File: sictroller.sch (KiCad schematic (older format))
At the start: 12 parts

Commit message: Placement almost complete
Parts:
- removed W2, W3, W4: TEST_1P, Measurement_Points:Measurement_Point_Round-SMD-Pad_Small, symbol TEST_1P
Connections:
- no-connect marks 0 -> 1
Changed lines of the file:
@@
-$EndComp
-$Comp
-L TEST_1P W2
-U 1 1 57A8E4FF
-P 4250 2000
-F 0 "W2" H 4300 2150 50  0000 L CNN
-F 1 "TEST_1P" H 4308 2029 50  0001 L CNN
-F 2 "Measurement_Points:Measurement_Point_Round-SMD-Pad_Small" H 4450 2000 50  0001 C CNN
-F 3 "" H 4450 2000 50  0000 C CNN
-	1    4250 2000
-	1    0    0    -1
-$EndComp
-$Comp
-L TEST_1P W3
-U 1 1 57A8E7A8
-P 4400 2100
-F 0 "W3" H 4450 2250 50  0000 L CNN
-F 1 "TEST_1P" H 4458 2129 50  0001 L CNN
-F 2 "Measurement_Points:Measurement_Point_Round-SMD-Pad_Small" H 4600 2100 50  0001 C CNN
-F 3 "" H 4600 2100 50  0000 C CNN
-	1    4400 2100
-	1    0    0    -1
-$EndComp
-$Comp
-L TEST_1P W4
-U 1 1 57A8EA5A
-P 4550 2200
-F 0 "W4" H 4600 2350 50  0000 L CNN
-F 1 "TEST_1P" H 4608 2229 50  0001 L CNN
-F 2 "Measurement_Points:Measurement_Point_Round-SMD-Pad_Small" H 4750 2200 50  0001 C CNN
-F 3 "" H 4750 2200 50  0000 C CNN
-	1    4550 2200
-	1    0    0    -1
 $EndComp
 $Comp
@@
 	1    0    0    -1
 $EndComp
+NoConn ~ 2800 1200
 $EndSCHEMATC

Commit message: Initial placement ~complete
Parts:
- removed W6, W7: TEST_1P, Measurement_Points:Measurement_Point_Round-TH_Small, symbol TEST_1P
- removed W8: TEST_1P, Measurement_Points:Measurement_Point_Round-SMD-Pad_Small, symbol TEST_1P
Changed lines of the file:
@@
 $EndComp
-$Comp
-L TEST_1P W6
-U 1 1 57A85972
-P 7300 2350
-F 0 "W6" H 7350 2450 50  0000 L CNN
-F 1 "TEST_1P" H 7358 2379 50  0001 L CNN
-F 2 "Measurement_Points:Measurement_Point_Round-TH_Small" H 7500 2350 50  0001 C CNN
-F 3 "" H 7500 2350 50  0000 C CNN
-	1    7300 2350
-	1    0    0    -1
-$EndComp
-$Comp
-L TEST_1P W7
-U 1 1 57A89327
-P 7500 2450
-F 0 "W7" H 7550 2600 50  0000 L CNN
-F 1 "TEST_1P" H 7558 2479 50  0001 L CNN
-F 2 "Measurement_Points:Measurement_Point_Round-TH_Small" H 7700 2450 50  0001 C CNN
-F 3 "" H 7700 2450 50  0000 C CNN
-	1    7500 2450
-	1    0    0    -1
-$EndComp
-$Comp
-L TEST_1P W8
-U 1 1 57A89F70
-P 7300 2650
-F 0 "W8" H 7350 2800 50  0000 L CNN
-F 1 "TEST_1P" H 7358 2679 50  0001 L CNN
-F 2 "Measurement_Points:Measurement_Point_Round-SMD-Pad_Small" H 7500 2650 50  0001 C CNN
-F 3 "" H 7500 2650 50  0000 C CNN
-	1    7300 2650
-	-1   0    0    1
-$EndComp
-Connection ~ 7300 2650
-Connection ~ 7500 2450
-Connection ~ 7300 2350
 $Comp
 L TEST_1P W1

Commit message: Add fiducials
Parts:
- added FID1, FID10, FID11, FID12, FID13, FID14, FID15, FID16, FID2, FID3, FID4, FID5, FID6, FID7, FID8, FID9, FID? (x4): Fiducial, sictroller:Fiducial_1mm_CopperTop, symbol Fiducial
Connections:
- no-connect marks 1 -> 0
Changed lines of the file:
@@
 $EndComp
 $Comp
-L GNDD #PWR1
+L GNDD #PWR01
 U 1 1 57A83FCA
 P 800 7550
-F 0 "#PWR1" H 800 7300 50  0001 C CNN
+F 0 "#PWR01" H 800 7300 50  0001 C CNN
 F 1 "GNDD" H 805 7377 50  0000 C CNN
 F 2 "" H 800 7550 50  0000 C CNN
@@
 $EndComp
 $Comp
-L GNDD #PWR2
+L GNDD #PWR02
 U 1 1 57A844D3
 P 1200 7550
-F 0 "#PWR2" H 1200 7300 50  0001 C CNN
+F 0 "#PWR02" H 1200 7300 50  0001 C CNN
 F 1 "GNDD" H 1205 7377 50  0000 C CNN
 F 2 "" H 1200 7550 50  0000 C CNN
@@
 Connection ~ 4100 2350
 $Comp
-L GNDA #PWR4
+L GNDA #PWR03
 U 1 1 5806E9BD
 P 2000 7550
-F 0 "#PWR4" H 2000 7300 50  0001 C CNN
+F 0 "#PWR03" H 2000 7300 50  0001 C CNN
 F 1 "GNDA" H 2000 7400 50  0000 C CNN
 F 2 "" H 2000 7550 50  0000 C CNN
@@
 $EndComp
 $Comp
-L GNDA #PWR3
+L GNDA #PWR04
 U 1 1 5806ED9E
 P 1600 7550
-F 0 "#PWR3" H 1600 7300 50  0001 C CNN
+F 0 "#PWR04" H 1600 7300 50  0001 C CNN
 F 1 "GNDA" H 1600 7400 50  0000 C CNN
 F 2 "" H 1600 7550 50  0000 C CNN
@@
 	1    0    0    -1
 $EndComp
-NoConn ~ 2800 1200
+$Comp
+L Fiducial FID1
+U 1 1 580C9076
+P 1950 4550
+F 0 "FID1" H 1960 4580 60  0000 C CNN
+F 1 "Fiducial" H 1940 4480 60  0000 C CNN
+F 2 "sictroller:Fiducial_1mm_CopperTop" H 1950 4550 60  0001 C CNN
+F 3 "" H 1950 4550 60  0001 C CNN
+	1    1950 4550
+	1    0    0    -1
+$EndComp
+$Comp
+L Fiducial FID2
+U 1 1 580C9CFA
+P 2550 4550
+F 0 "FID2" H 2560 4580 60  0000 C CNN
+F 1 "Fiducial" H 2540 4480 60  0000 C CNN
+F 2 "sictroller:Fiducial_1mm_CopperTop" H 2550 4550 60  0001 C CNN
+F 3 "" H 2550 4550 60  0001 C CNN
+	1    2550 4550
+	1    0    0    -1
+$EndComp
+$Comp
+L Fiducial FID3
+U 1 1 580CA196
+P 3150 4550
+F 0 "FID3" H 3160 4580 60  0000 C CNN
+F 1 "Fiducial" H 3140 4480 60  0000 C CNN
+F 2 "sictroller:Fiducial_1mm_CopperTop" H 3150 4550 60  0001 C CNN
+F 3 "" H 3150 4550 60  0001 C CNN
+	1    3150 4550
+	1    0    0    -1
+$EndComp
+$Comp
+L Fiducial FID4
+U 1 1 580CA19C
+P 3750 4550
+F 0 "FID4" H 3760 4580 60  0000 C CNN
+F 1 "Fiducial" H 3740 4480 60  0000 C CNN
+F 2 "sictroller:Fiducial_1mm_CopperTop" H 3750 4550 60  0001 C CNN
+F 3 "" H 3750 4550 60  0001 C CNN
+	1    3750 4550
+	1    0    0    -1
+$EndComp
+$Comp
+L Fiducial FID7
+U 1 1 580CA452
+P 3150 4950
+F 0 "FID7" H 3160 4980 60  0000 C CNN
+F 1 "Fiducial" H 3140 4880 60  0000 C CNN
+F 2 "sictroller:Fiducial_1mm_CopperTop" H 3150 4950 60  0001 C CNN
+F 3 "" H 3150 4950 60  0001 C CNN
+	1    3150 4950
+	1    0    0    -1
+$EndComp
+$Comp
+L Fiducial FID8
+U 1 1 580CA458
+P 3750 4950
+F 0 "FID8" H 3760 4980 60  0000 C CNN
+F 1 "Fiducial" H 3740 4880 60  0000 C CNN
+F 2 "sictroller:Fiducial_1mm_CopperTop" H 3750 4950 60  0001 C CNN
+F 3 "" H 3750 4950 60  0001 C CNN
+	1    3750 4950
+	1    0    0    -1
+$EndComp
+$Comp
+L Fiducial FID5
+U 1 1 580CA6D6
+P 1950 4950
+F 0 "FID5" H 1960 4980 60  0000 C CNN
+F 1 "Fiducial" H 1940 4880 60  0000 C CNN
+F 2 "sictroller:Fiducial_1mm_CopperTop" H 1950 4950 60  0001 C CNN
+F 3 "" H 1950 4950 60  0001 C CNN
+	1    1950 4950
+	1    0    0    -1
+$EndComp
+$Comp
+L Fiducial FID6
+U 1 1 580CA6DC
+P 2550 4950
+F 0 "FID6" H 2560 4980 60  0000 C CNN
+F 1 "Fiducial" H 2540 4880 60  0000 C CNN
+F 2 "sictroller:Fiducial_1mm_CopperTop" H 2550 4950 60  0001 C CNN
+F 3 "" H 2550 4950 60  0001 C CNN
+	1    2550 4950
+	1    0    0    -1
+$EndComp
+$Comp
+L Fiducial FID11
+U 1 1 580CC37C
+P 3150 5350
+F 0 "FID11" H 3160 5380 60  0000 C CNN
+F 1 "Fiducial" H 3140 5280 60  0000 C CNN
+F 2 "sictroller:Fiducial_1mm_CopperTop" H 3150 5350 60  0001 C CNN
+F 3 "" H 3150 5350 60  0001 C CNN
+	1    3150 5350
+	1    0    0    -1
+$EndComp
+$Comp
+L Fiducial FID12
+U 1 1 580CC382
+P 3750 5350
+F 0 "FID12" H 3760 5380 60  0000 C CNN
+F 1 "Fiducial" H 3740 5280 60  0000 C CNN
+F 2 "sictroller:Fiducial_1mm_CopperTop" H 3750 5350 60  0001 C CNN
+F 3 "" H 3750 5350 60  0001 C CNN
+	1    3750 5350
+	1    0    0    -1
+$EndComp
+$Comp
+L Fiducial FID9
+U 1 1 580CC388
+P 1950 5350
+F 0 "FID9" H 1960 5380 60  0000 C CNN
+F 1 "Fiducial" H 1940 5280 60  0000 C CNN
+F 2 "sictroller:Fiducial_1mm_CopperTop" H 1950 5350 60  0001 C CNN
+F 3 "" H 1950 5350 60  0001 C CNN
+	1    1950 5350
+	1    0    0    -1
+$EndComp
+$Comp
+L Fiducial FID10
+U 1 1 580CC38E
+P 2550 5350
+F 0 "FID10" H 2560 5380 60  0000 C CNN
+F 1 "Fiducial" H 2540 5280 60  0000 C CNN
+F 2 "sictroller:Fiducial_1mm_CopperTop" H 2550 5350 60  0001 C CNN
+F 3 "" H 2550 5350 60  0001 C CNN
+	1    2550 5350
+	1    0    0    -1
+$EndComp
+$Comp
+L Fiducial FID15
+U 1 1 580CCCE0
+P 3150 5750
+F 0 "FID15" H 3160 5780 60  0000 C CNN
+F 1 "Fiducial" H 3140 5680 60  0000 C CNN
+F 2 "sictroller:Fiducial_1mm_CopperTop" H 3150 5750 60  0001 C CNN
+F 3 "" H 3150 5750 60  0001 C CNN
+	1    3150 5750
+	1    0    0    -1
+$EndComp
+$Comp
+L Fiducial FID16
+U 1 1 580CCCE6
+P 3750 5750
+F 0 "FID16" H 3760 5780 60  0000 C CNN
+F 1 "Fiducial" H 3740 5680 60  0000 C CNN
+F 2 "sictroller:Fiducial_1mm_CopperTop" H 3750 5750 60  0001 C CNN
+F 3 "" H 3750 5750 60  0001 C CNN
+	1    3750 5750
+	1    0    0    -1
+$EndComp
+$Comp
+L Fiducial FID13
+U 1 1 580CCCEC
+P 1950 5750
+F 0 "FID13" H 1960 5780 60  0000 C CNN
+F 1 "Fiducial" H 1940 5680 60  0000 C CNN
+F 2 "sictroller:Fiducial_1mm_CopperTop" H 1950 5750 60  0001 C CNN
+F 3 "" H 1950 5750 60  0001 C CNN
+	1    1950 5750
+	1    0    0    -1
+$EndComp
+$Comp
+L Fiducial FID14
+U 1 1 580CCCF2
+P 2550 5750
+F 0 "FID14" H 2560 5780 60  0000 C CNN
+F 1 "Fiducial" H 2540 5680 60  0000 C CNN
+F 2 "sictroller:Fiducial_1mm_CopperTop" H 2550 5750 60  0001 C CNN
+F 3 "" H 2550 5750 60  0001 C CNN
+	1    2550 5750
+	1    0    0    -1
+$EndComp
+$Comp
+L Fiducial FID?
+U 1 1 580CDCBE
+P 3150 6150
+F 0 "FID?" H 3160 6180 60  0000 C CNN
+F 1 "Fiducial" H 3140 6080 60  0000 C CNN
+F 2 "sictroller:Fiducial_1mm_CopperTop" H 3150 6150 60  0001 C CNN
+F 3 "" H 3150 6150 60  0001 C CNN
+	1    3150 6150
+	1    0    0    -1
+$EndComp
+$Comp
+L Fiducial FID?
+U 1 1 580CDCC4
+P 3750 6150
+F 0 "FID?" H 3760 6180 60  0000 C CNN
+F 1 "Fiducial" H 3740 6080 60  0000 C CNN
+F 2 "sictroller:Fiducial_1mm_CopperTop" H 3750 6150 60  0001 C CNN
+F 3 "" H 3750 6150 60  0001 C CNN
+	1    3750 6150
+	1    0    0    -1
+$EndComp
+$Comp
+L Fiducial FID?
+U 1 1 580CDCCA
+P 1950 6150
+F 0 "FID?" H 1960 6180 60  0000 C CNN
+F 1 "Fiducial" H 1940 6080 60  0000 C CNN
+F 2 "sictroller:Fiducial_1mm_CopperTop" H 1950 6150 60  0001 C CNN
+F 3 "" H 1950 6150 60  0001 C CNN
+	1    1950 6150
+	1    0    0    -1
+$EndComp
+$Comp
+L Fiducial FID?
+U 1 1 580CDCD0
+P 2550 6150
+F 0 "FID?" H 2560 6180 60  0000 C CNN
+F 1 "Fiducial" H 2540 6080 60  0000 C CNN
+F 2 "sictroller:Fiducial_1mm_CopperTop" H 2550 6150 60  0001 C CNN
+F 3 "" H 2550 6150 60  0001 C CNN
+	1    2550 6150
+	1    0    0    -1
+$EndComp
 $EndSCHEMATC

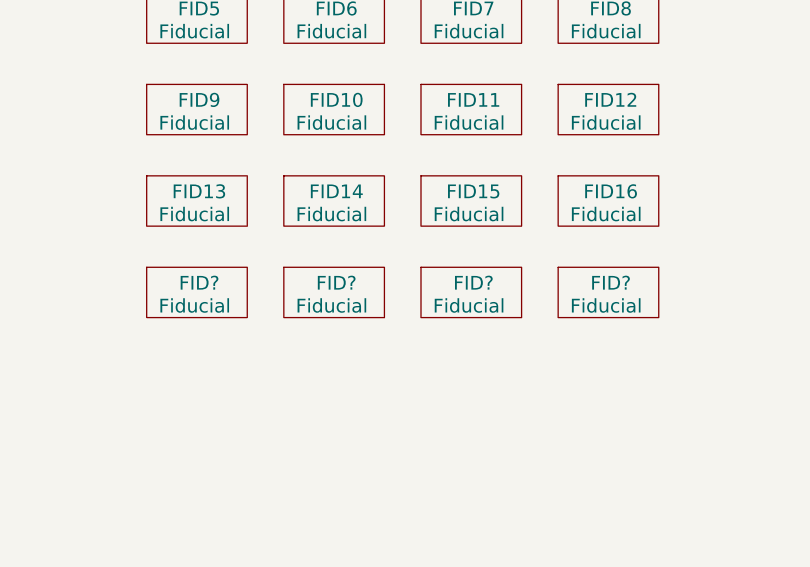
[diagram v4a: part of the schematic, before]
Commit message: Add M2 mounting holes for cover
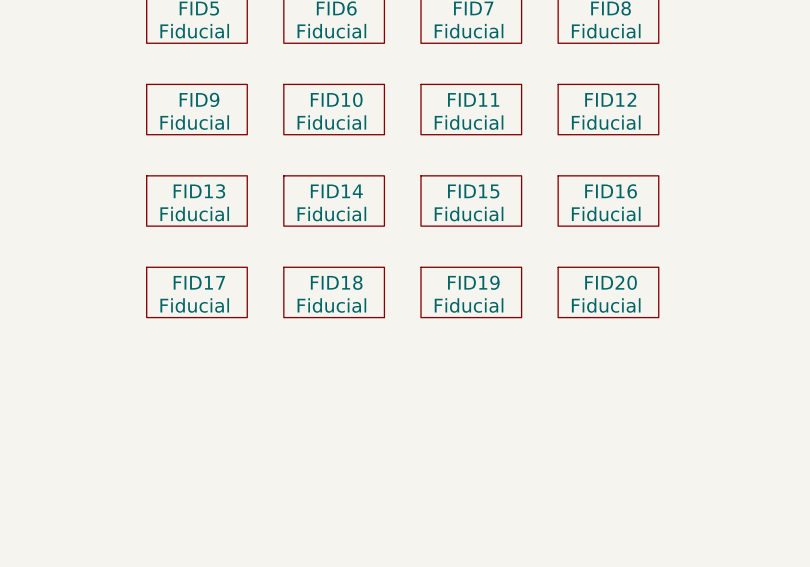
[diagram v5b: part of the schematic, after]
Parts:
- gave numbers to parts that had none: 4
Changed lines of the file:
@@
 $EndComp
 $Comp
-L Fiducial FID?
+L Fiducial FID19
 U 1 1 580CDCBE
 P 3150 6150
-F 0 "FID?" H 3160 6180 60  0000 C CNN
+F 0 "FID19" H 3160 6180 60  0000 C CNN
 F 1 "Fiducial" H 3140 6080 60  0000 C CNN
 F 2 "sictroller:Fiducial_1mm_CopperTop" H 3150 6150 60  0001 C CNN
@@
 $EndComp
 $Comp
-L Fiducial FID?
+L Fiducial FID20
 U 1 1 580CDCC4
 P 3750 6150
-F 0 "FID?" H 3760 6180 60  0000 C CNN
+F 0 "FID20" H 3760 6180 60  0000 C CNN
 F 1 "Fiducial" H 3740 6080 60  0000 C CNN
 F 2 "sictroller:Fiducial_1mm_CopperTop" H 3750 6150 60  0001 C CNN
@@
 $EndComp
 $Comp
-L Fiducial FID?
+L Fiducial FID17
 U 1 1 580CDCCA
 P 1950 6150
-F 0 "FID?" H 1960 6180 60  0000 C CNN
+F 0 "FID17" H 1960 6180 60  0000 C CNN
 F 1 "Fiducial" H 1940 6080 60  0000 C CNN
 F 2 "sictroller:Fiducial_1mm_CopperTop" H 1950 6150 60  0001 C CNN
@@
 $EndComp
 $Comp
-L Fiducial FID?
+L Fiducial FID18
 U 1 1 580CDCD0
 P 2550 6150
-F 0 "FID?" H 2560 6180 60  0000 C CNN
+F 0 "FID18" H 2560 6180 60  0000 C CNN
 F 1 "Fiducial" H 2540 6080 60  0000 C CNN
 F 2 "sictroller:Fiducial_1mm_CopperTop" H 2550 6150 60  0001 C CNN

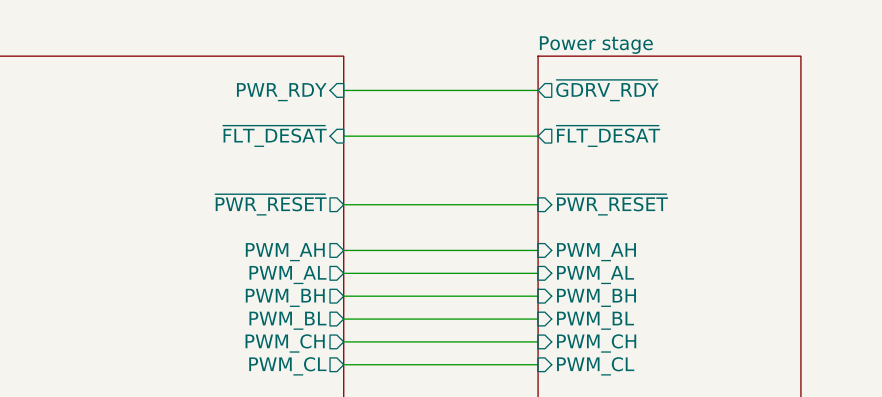
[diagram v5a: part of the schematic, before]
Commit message: V2.1: Fixes for V2.0 bugs
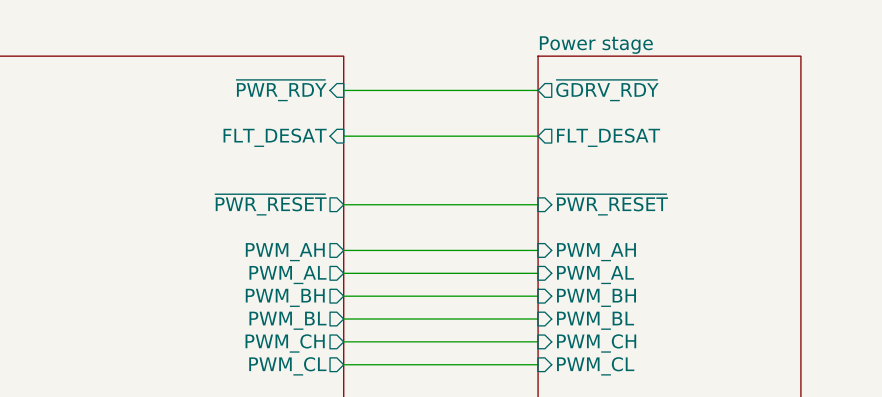
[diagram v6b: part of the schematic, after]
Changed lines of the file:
@@
 F12 "PWM_BL" O R 7100 2650 60
 F13 "PWM_CL" O R 7100 2850 60
-F14 "~FLT_DESAT" I R 7100 1850 60
-F15 "PWR_RDY" I R 7100 1650 60
-F16 "~PWR_RESET" O R 7100 2150 60
-F17 "~IFB_A" I L 4750 2350 60
-F18 "TEMP_PWM" I L 4750 1650 60
-F19 "TEMP_EN" O L 4750 1750 60
+F14 "~PWR_RESET" O R 7100 2150 60
+F15 "~IFB_A" I L 4750 2350 60
+F16 "TEMP_PWM" I L 4750 1650 60
+F17 "TEMP_EN" O L 4750 1750 60
+F18 "FLT_DESAT" I R 7100 1850 60
+F19 "~PWR_RDY" I R 7100 1650 60
 $EndSheet
 $Sheet
@@
 F7 "PWM_CH" I L 7950 2750 60
 F8 "PWM_CL" I L 7950 2850 60
-F9 "~FLT_DESAT" O L 7950 1850 60
-F10 "~GDRV_RDY" O L 7950 1650 60
+F9 "~GDRV_RDY" O L 7950 1650 60
+F10 "FLT_DESAT" O L 7950 1850 60
 $EndSheet
 Wire Wire Line
